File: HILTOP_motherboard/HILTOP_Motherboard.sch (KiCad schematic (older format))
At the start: 202 parts, among them J1 BACKPLANE_PWR, J10 HDMI, J11 DISP_PWR, J12 DISPLAY_PORT, J14 VADJ_B, J15 VADJ_A, J16 SOFT_START_PWR, J17 PWR_LED, J18 USB_B, J19 Micro_SD_Card, J2 ATX_MOLEX_02X12, J20 CAMERA_PORT, J21 EXT_FAN, J22 BACKPLANE_LV_PWR, J23 EXT_FAN, J26 IO_EXP, J3 SATA, J4 USB_A_DOUBLE, J5 USB FRONT PANEL, J6 CAN, J7 RS485, J8 EXT_TEMP_MON, J9 RJ45-TRANS_SI-61001-F, U1 LM337BD2TG, U25 STM6719SFWB6F, U39 MCP23017

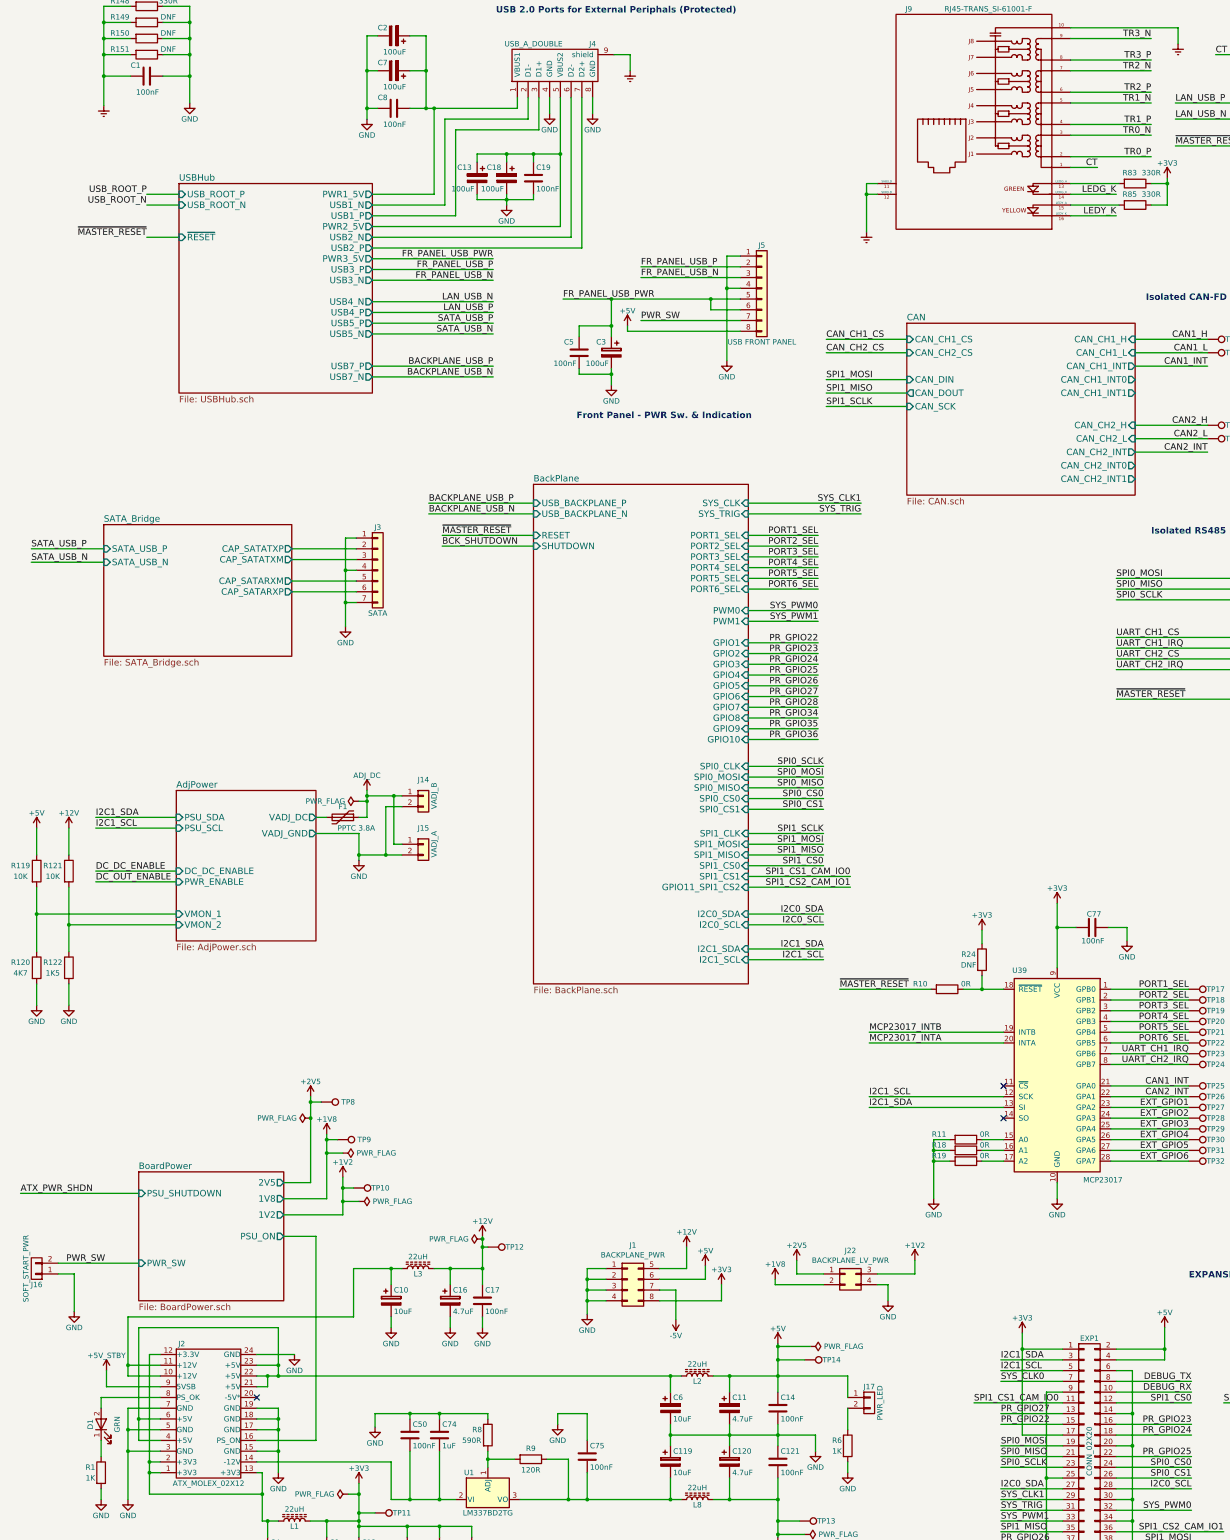
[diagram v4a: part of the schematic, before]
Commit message: DRC checks complete, all errors and warnings cleared. BOM created and parts rationalised.
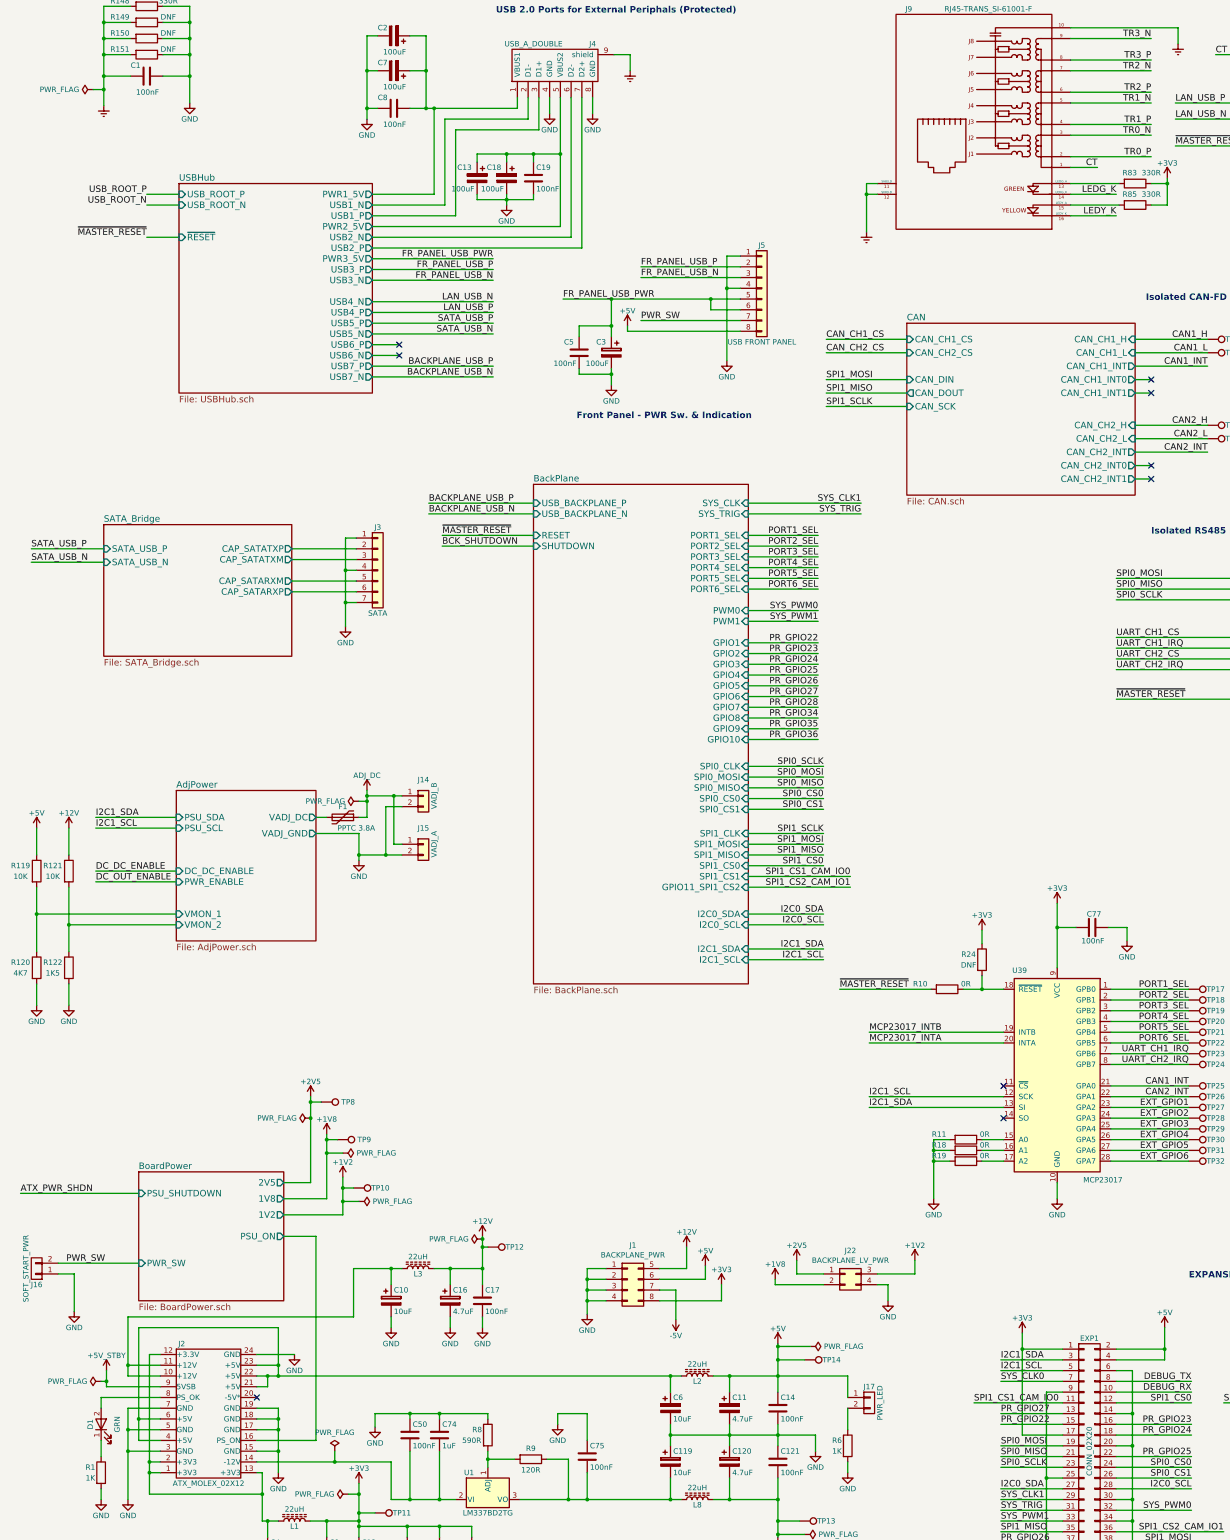
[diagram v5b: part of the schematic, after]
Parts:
- C1: Devtank 105-002 -> 105-020
- C11, C120, C16: Devtank 108-002 -> 108-001
- C13, C18, C2, C3, C7: Devtank 108-002 -> 108-003
- C51: footprint Capacitor_SMD:C_0201_0603Metric -> Capacitor_SMD:C_0402_1005Metric; Devtank 105-002 -> 105-019
- J11: Devtank 710-006 -> 710-016
- R245, R246, R247, R248, R249, R54: Devtank 101-049 -> 101-503
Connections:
- no-connect marks 8 -> 14
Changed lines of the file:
@@
 F18 "PWR2_5V" O R 4075 3100 60
 F19 "PWR1_5V" O R 4075 2800 60
+F20 "USB6_P" O R 4075 4200 60
+F21 "USB6_N" O R 4075 4300 60
 $EndSheet
 $Sheet
@@
 F 2 "Connector_Molex:Molex_KK-254_AE-6410-05A_1x05_P2.54mm_Vertical" H 20800 12050 50  0001 C CNN
 F 3 "" H 20800 12050 50  0000 C CNN
-F 4 "710-006" H 20800 12050 60  0001 C CNN "Devtank"
+F 4 "710-016" H 20800 12050 60  0001 C CNN "Devtank"
 	1    20800 12050
 	0    1    1    0
@@
 F 2 "Capacitor_SMD:CP_Elec_5x5.3" H 7438 13950 50  0001 C CNN
 F 3 "" H 7400 14100 50  0000 C CNN
-F 4 "108-002" H 7400 14100 60  0001 C CNN "Devtank"
+F 4 "108-001" H 7400 14100 60  0001 C CNN "Devtank"
 	1    7400 14100
 	1    0    0    -1
@@
 F 2 "Capacitor_SMD:CP_Elec_5x5.3" H 4838 12950 50  0001 C CNN
 F 3 "" H 4800 13100 50  0000 C CNN
-F 4 "108-002" H 4800 13100 60  0001 C CNN "Devtank"
+F 4 "108-001" H 4800 13100 60  0001 C CNN "Devtank"
 	1    4800 13100
 	1    0    0    -1
@@
 F 2 "Capacitor_SMD:CP_Elec_5x5.3" H 7438 14450 50  0001 C CNN
 F 3 "" H 7400 14600 50  0000 C CNN
-F 4 "108-002" H 7400 14600 60  0001 C CNN "Devtank"
+F 4 "108-001" H 7400 14600 60  0001 C CNN "Devtank"
 	1    7400 14600
 	1    0    0    -1
@@
 F 0 "C51" H 19375 2500 50  0000 L CNN
 F 1 "100nF" H 19375 2300 50  0000 L CNN
-F 2 "Capacitor_SMD:C_0201_0603Metric" H 19388 2250 50  0001 C CNN
+F 2 "Capacitor_SMD:C_0402_1005Metric" H 19388 2250 50  0001 C CNN
 F 3 "" H 19350 2400 50  0000 C CNN
-F 4 "105-002" H 19350 2400 60  0001 C CNN "Devtank"
+F 4 "105-019" H 19350 2400 60  0001 C CNN "Devtank"
 	1    19350 2400
 	1    0    0    -1
@@
 F 2 "Capacitor_SMD:CP_Elec_6.3x7.7" H 6338 4125 50  0001 C CNN
 F 3 "" H 6300 4275 50  0000 C CNN
-F 4 "108-002" H 6300 4275 60  0001 C CNN "Devtank"
+F 4 "108-003" H 6300 4275 60  0001 C CNN "Devtank"
 	1    6300 4275
 	-1   0    0    -1
@@
 F 2 "Capacitor_SMD:CP_Elec_6.3x7.7" H 5363 2500 50  0001 C CNN
 F 3 "" H 5325 2650 50  0000 C CNN
-F 4 "108-002" H 5325 2650 60  0001 C CNN "Devtank"
+F 4 "108-003" H 5325 2650 60  0001 C CNN "Devtank"
 	1    5325 2650
 	-1   0    0    -1
@@
 F 2 "Capacitor_SMD:CP_Elec_6.3x7.7" H 4313 1500 50  0001 C CNN
 F 3 "" H 4275 1650 50  0000 C CNN
-F 4 "108-002" H 4275 1650 60  0001 C CNN "Devtank"
+F 4 "108-003" H 4275 1650 60  0001 C CNN "Devtank"
 	1    4275 1650
 	0    1    -1   0
@@
 F 2 "Capacitor_SMD:CP_Elec_6.3x7.7" H 5088 2500 50  0001 C CNN
 F 3 "" H 5050 2650 50  0000 C CNN
-F 4 "108-002" H 5050 2650 60  0001 C CNN "Devtank"
+F 4 "108-003" H 5050 2650 60  0001 C CNN "Devtank"
 	1    5050 2650
 	-1   0    0    -1
@@
 F 2 "Capacitor_SMD:CP_Elec_6.3x7.7" H 4313 1175 50  0001 C CNN
 F 3 "" H 4275 1325 50  0000 C CNN
-F 4 "108-002" H 4275 1325 60  0001 C CNN "Devtank"
+F 4 "108-003" H 4275 1325 60  0001 C CNN "Devtank"
 	1    4275 1325
 	0    1    -1   0
@@
 F 2 "Capacitor_SMD:C_1210_3225Metric" H 2013 1550 50  0001 C CNN
 F 3 "" H 1975 1700 50  0000 C CNN
-F 4 "105-002" V 1975 1700 60  0001 C CNN "Devtank"
+F 4 "105-020" V 1975 1700 60  0001 C CNN "Devtank"
 	1    1975 1700
 	0    1    1    0
@@
 	1900 12100 800  12100
 Wire Wire Line
-	1600 13750 1600 13900
+	1600 13750 1600 13850
 Wire Wire Line
 	1150 12750 1900 12750
@@
 	2375 1700 2375 1950
 Wire Wire Line
-	1575 1700 1575 1975
+	1575 1700 1575 1825
 Wire Wire Line
 	4575 1650 4575 2000
@@
 	4250 14950 4250 14600
 Wire Wire Line
-	4250 14600 3000 14600
+	4250 14600 3725 14600
 Wire Wire Line
 	5150 14500 5150 14575
@@
 F 2 "Resistor_SMD:R_0402_1005Metric" V 14080 10700 50  0001 C CNN
 F 3 "" H 14150 10700 50  0000 C CNN
-F 4 "101-049" H 14150 10700 60  0001 C CNN "Devtank"
+F 4 "101-503" H 14150 10700 60  0001 C CNN "Devtank"
 	1    14150 10700
 	0    1    1    0
@@
 F 2 "Resistor_SMD:R_0402_1005Metric" V 14080 10800 50  0001 C CNN
 F 3 "" H 14150 10800 50  0000 C CNN
-F 4 "101-049" H 14150 10800 60  0001 C CNN "Devtank"
+F 4 "101-503" H 14150 10800 60  0001 C CNN "Devtank"
 	1    14150 10800
 	0    1    1    0
@@
 F 2 "Resistor_SMD:R_0402_1005Metric" V 14080 10900 50  0001 C CNN
 F 3 "" H 14150 10900 50  0000 C CNN
-F 4 "101-049" H 14150 10900 60  0001 C CNN "Devtank"
+F 4 "101-503" H 14150 10900 60  0001 C CNN "Devtank"
 	1    14150 10900
 	0    1    1    0
@@
 F 2 "Resistor_SMD:R_0402_1005Metric" V 14080 11000 50  0001 C CNN
 F 3 "" H 14150 11000 50  0000 C CNN
-F 4 "101-049" H 14150 11000 60  0001 C CNN "Devtank"
+F 4 "101-503" H 14150 11000 60  0001 C CNN "Devtank"
 	1    14150 11000
 	0    1    1    0
@@
 F 2 "Resistor_SMD:R_0402_1005Metric" V 14080 11100 50  0001 C CNN
 F 3 "" H 14150 11100 50  0000 C CNN
-F 4 "101-049" H 14150 11100 60  0001 C CNN "Devtank"
+F 4 "101-503" H 14150 11100 60  0001 C CNN "Devtank"
 	1    14150 11100
 	0    1    1    0
@@
 F 2 "Resistor_SMD:R_0402_1005Metric" V 14080 11200 50  0001 C CNN
 F 3 "" H 14150 11200 50  0000 C CNN
-F 4 "101-049" H 14150 11200 60  0001 C CNN "Devtank"
+F 4 "101-503" H 14150 11200 60  0001 C CNN "Devtank"
 	1    14150 11200
 	0    1    1    0
@@
 Wire Wire Line
 	4075 3400 5200 3400
+Wire Wire Line
+	11175 4525 11325 4525
+Wire Wire Line
+	11175 4650 11325 4650
+Wire Wire Line
+	11175 5325 11325 5325
+Wire Wire Line
+	11175 5450 11325 5450
+NoConn ~ 11325 4525
+NoConn ~ 11325 4650
+NoConn ~ 11325 5325
+NoConn ~ 11325 5450
+$Comp
+L power:PWR_FLAG #FLG0121
+U 1 1 5DD2AF96
+P 1475 1825
+F 0 "#FLG0121" H 1475 1900 50  0001 C CNN
+F 1 "PWR_FLAG" V 1475 1953 50  0000 L CNN
+F 2 "" H 1475 1825 50  0001 C CNN
+F 3 "" H 1475 1825 50  0001 C CNN
+	1    1475 1825
+	0    -1   -1   0
+$EndComp
+Wire Wire Line
+	1475 1825 1575 1825
+Connection ~ 1575 1825
+Wire Wire Line
+	1575 1825 1575 1975
+Wire Wire Line
+	4075 4200 4325 4200
+Wire Wire Line
+	4075 4300 4325 4300
+NoConn ~ 4325 4200
+NoConn ~ 4325 4300
+$Comp
+L power:PWR_FLAG #FLG0129
+U 1 1 5E6340CA
+P 3725 14500
+F 0 "#FLG0129" H 3725 14575 50  0001 C CNN
+F 1 "PWR_FLAG" H 3725 14674 50  0000 C CNN
+F 2 "" H 3725 14500 50  0001 C CNN
+F 3 "" H 3725 14500 50  0001 C CNN
+	1    3725 14500
+	1    0    0    -1
+$EndComp
+Wire Wire Line
+	3725 14500 3725 14600
+Connection ~ 3725 14600
+Wire Wire Line
+	3725 14600 3000 14600
+$Comp
+L power:PWR_FLAG #FLG0130
+U 1 1 5E77340E
+P 1550 13850
+F 0 "#FLG0130" H 1550 13925 50  0001 C CNN
+F 1 "PWR_FLAG" V 1550 13978 50  0000 L CNN
+F 2 "" H 1550 13850 50  0001 C CNN
+F 3 "" H 1550 13850 50  0001 C CNN
+	1    1550 13850
+	0    -1   -1   0
+$EndComp
+Wire Wire Line
+	1550 13850 1600 13850
+Connection ~ 1600 13850
+Wire Wire Line
+	1600 13850 1600 13900
 $EndSCHEMATC

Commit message: tracking updates
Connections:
- net SATA_Bridge/CAP_SATARXM renamed SATA_Bridge/CAP_SATARX_N
- net SATA_Bridge/CAP_SATARXP renamed SATA_Bridge/CAP_SATARX_P
- net SATA_Bridge/CAP_SATATXM renamed SATA_Bridge/CAP_SATATX_N
- net SATA_Bridge/CAP_SATATXP renamed SATA_Bridge/CAP_SATATX_P
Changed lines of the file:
@@
 F2 "SATA_USB_P" I L 1575 6100 60
 F3 "SATA_USB_N" I L 1575 6225 60
-F4 "CAP_SATATXM" O R 3325 6200 60
-F5 "CAP_SATATXP" O R 3325 6100 60
-F6 "CAP_SATARXM" O R 3325 6400 60
-F7 "CAP_SATARXP" O R 3325 6500 60
+F4 "CAP_SATATX_N" O R 3325 6200 60
+F5 "CAP_SATATX_P" O R 3325 6100 60
+F6 "CAP_SATARX_N" O R 3325 6400 60
+F7 "CAP_SATARX_P" O R 3325 6500 60
 $EndSheet
 $Comp

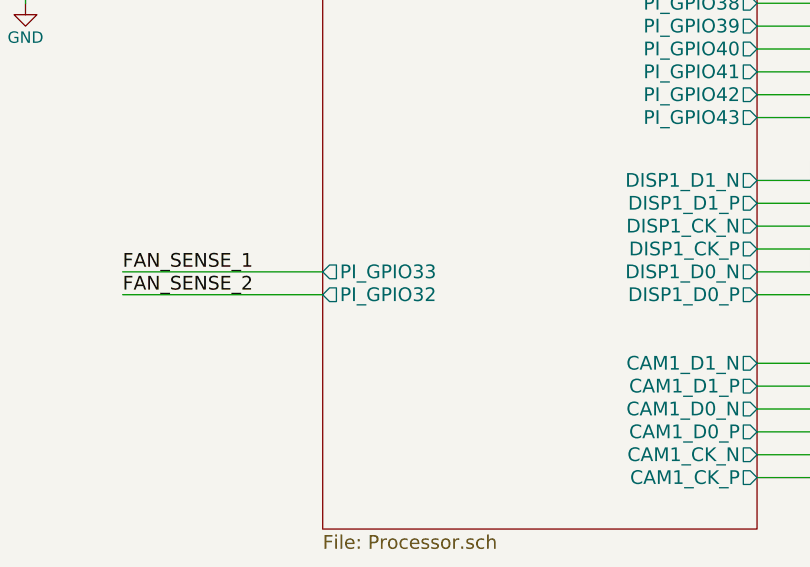
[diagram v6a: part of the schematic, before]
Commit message: 90% complete on backplane and IO connectors
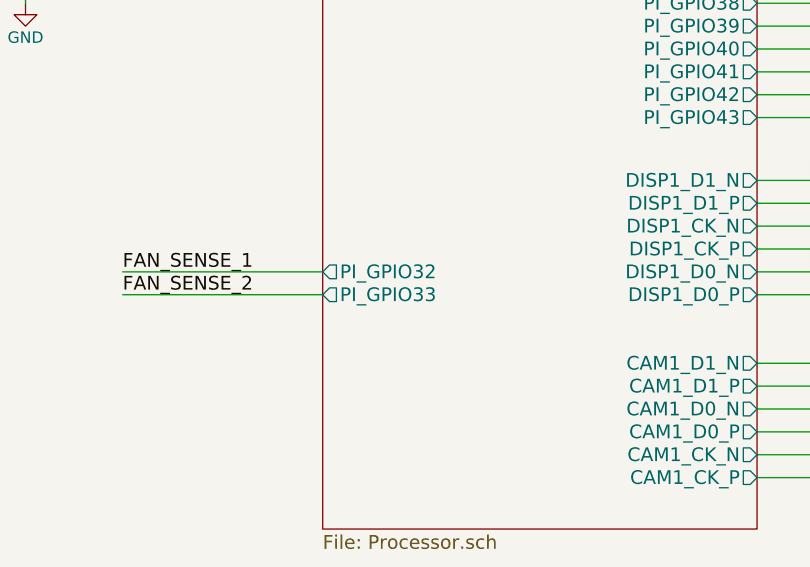
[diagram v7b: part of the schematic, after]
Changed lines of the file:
@@
 F16 "PI_GPIO30" O R 18200 10775 60
 F17 "PI_GPIO31" O R 18200 10875 60
-F18 "PI_GPIO32" O L 16300 12650 60
-F19 "PI_GPIO33" O L 16300 12550 60
+F18 "PI_GPIO32" O L 16300 12550 60
+F19 "PI_GPIO33" O L 16300 12650 60
 F20 "PI_GPIO34" O R 18200 10200 60
 F21 "PI_GPIO35" O R 18200 10300 60

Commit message: nearly there, drc errors all resolved!
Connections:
- net at C4.1, J2.1 (+3V3), J2.13 (+3V3)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: no longer J2.12 (+3.3V)
- no-connect marks 14 -> 15
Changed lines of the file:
@@
 Wire Wire Line
 	21700 1900 21700 2050
-Connection ~ 2000 14600
-Wire Wire Line
-	2100 13600 2000 13600
 Wire Wire Line
 	3350 13600 3000 13600
@@
 	2000 14700 2100 14700
 Wire Wire Line
-	2000 13600 2000 14600
-Wire Wire Line
 	2000 14900 3050 14900
 Connection ~ 3200 14200
@@
 Wire Wire Line
 	1600 13850 1600 13900
+NoConn ~ 2100 13600
 $EndSCHEMATC
